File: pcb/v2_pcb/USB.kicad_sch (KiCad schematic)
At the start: 17 parts, among them IC1 AP33772SDKZ-13-FA01, J2 USB_C_Receptacle_USB2.0_16P, Q1 NMOS, Q2 NMOS, U4 TPD8S300ARUKR

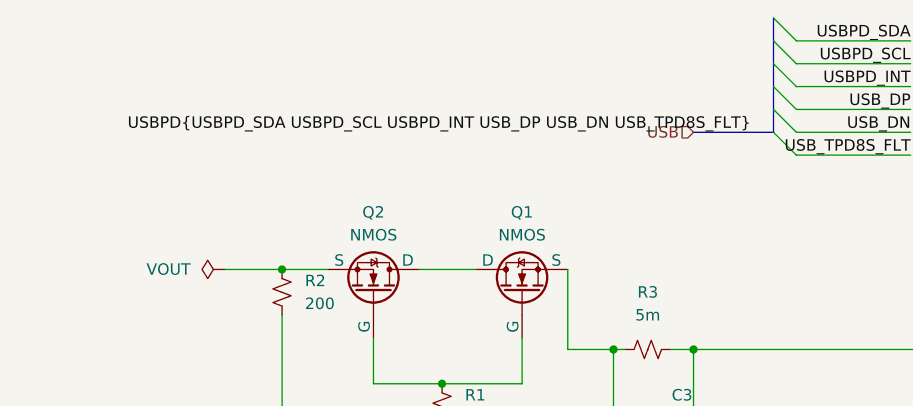
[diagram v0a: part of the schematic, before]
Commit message: done with max17320
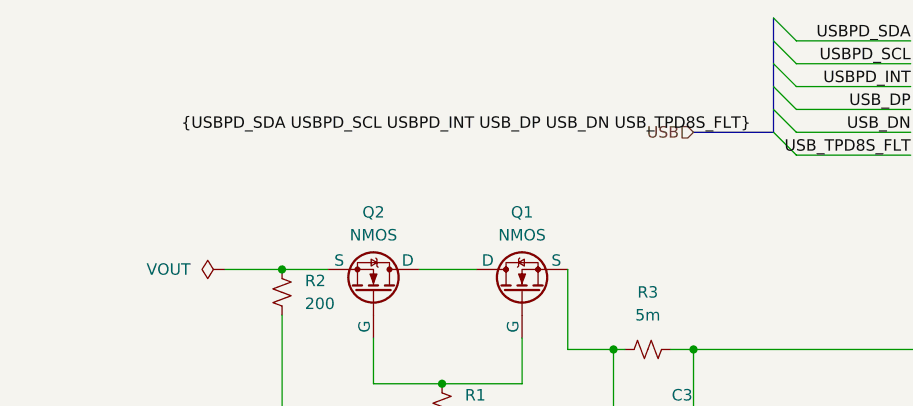
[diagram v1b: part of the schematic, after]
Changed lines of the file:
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@@
 		)
 	)
-	(label "USBPD{USBPD_SDA USBPD_SCL USBPD_INT USB_DP USB_DN USB_TPD8S_FLT}"
+	(label "{USBPD_SDA USBPD_SCL USBPD_INT USB_DP USB_DN USB_TPD8S_FLT}"
 		(at 97.79 50.8 180)
 		(effects

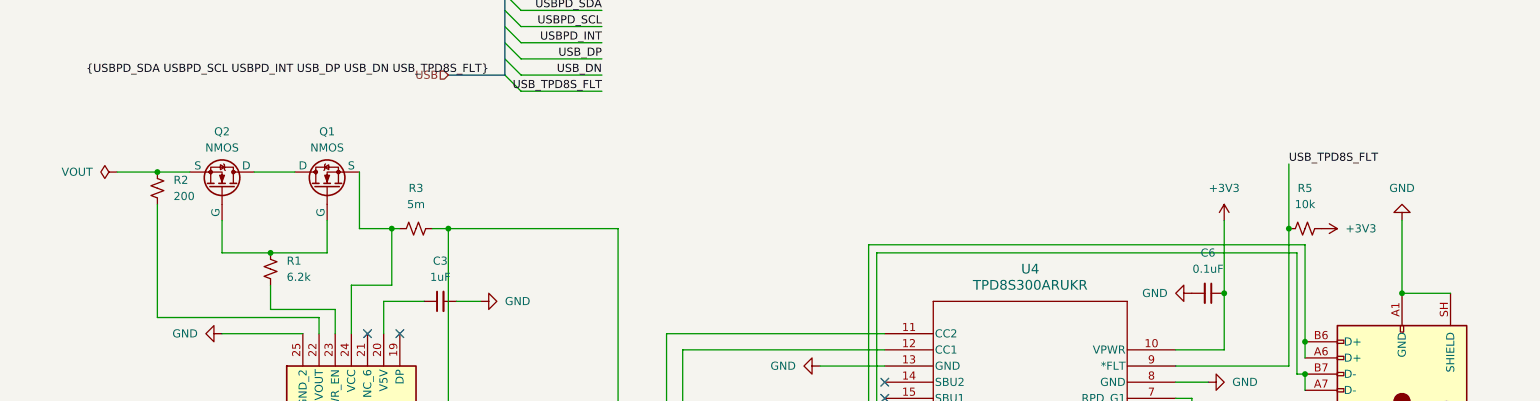
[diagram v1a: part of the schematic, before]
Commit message: add rpls for 1v8, 5v
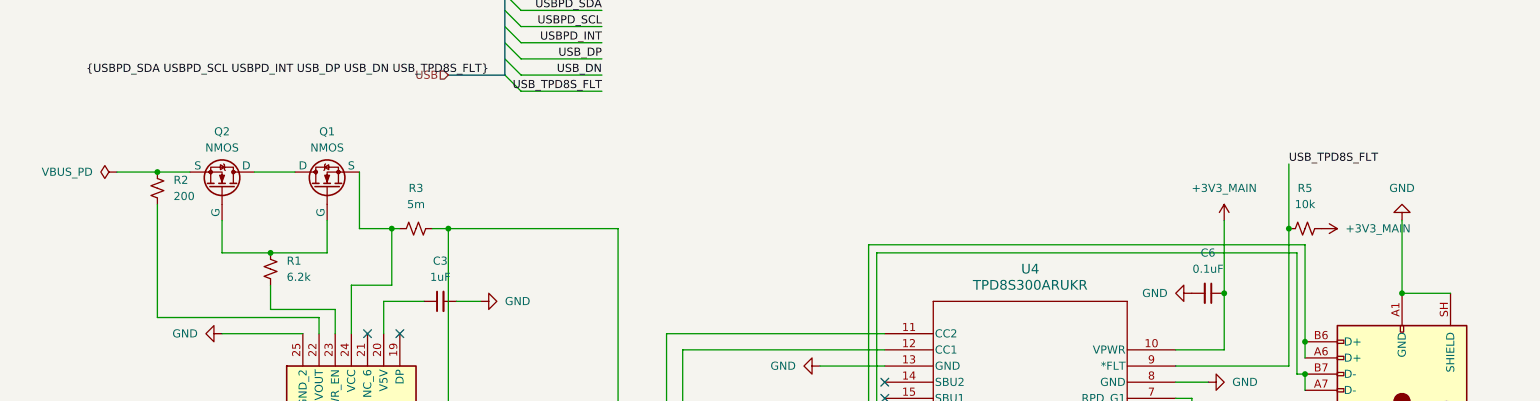
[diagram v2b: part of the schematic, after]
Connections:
- net +3V3 renamed +3V3_MAIN
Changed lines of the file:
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@@
 			)
 		)
-		(property "Value" "+3V3"
+		(property "Value" "+3V3_MAIN"
 			(at 213.36 68.58 0)
 			(show_name no)
@@
 			)
 		)
-		(property "Value" "+3V3"
+		(property "Value" "+3V3_MAIN"
 			(at 232.41 74.9299 90)
 			(show_name no)
@@
 			)
 		)
-		(property "Value" "VOUT"
+		(property "Value" "VBUS_PD"
 			(at 35.56 66.0399 90)
 			(show_name no)

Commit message: pcb done
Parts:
- removed Q1, Q2: NMOS, symbol Simulation_SPICE:NMOS
- added C230: 1uF 35V X7R, Capacitor_SMD:C_0805_2012Metric, symbol Device:C_Small
- added C231, C232: 100nF, Capacitor_SMD:C_0603_1608Metric, symbol Device:C_Small
- added C253: 100nF 10V X7R, Capacitor_SMD:C_0603_1608Metric, symbol Device:C_Small
- added C254: 1nF 10V X7R, Capacitor_SMD:C_0603_1608Metric, symbol Device:C_Small
- added Q1, Q2: CSD18540Q5B, open-race-v2:VSON-CLIP-8_DNK_5x6mm, symbol open-race-v2:CSD18540Q5B
- added R241, R242: 5.1k 1%, Resistor_SMD:R_0603_1608Metric, symbol Device:R_Small_US
- added R243: 10k, Resistor_SMD:R_0603_1608Metric, symbol Device:R_Small_US
- added R249: 100k, Resistor_SMD:R_0603_1608Metric, symbol Device:R_Small_US
- added R250: 88.7k 1%, Resistor_SMD:R_0603_1608Metric, symbol Device:R_Small_US
- added R251: 10.0k 1%, Resistor_SMD:R_0603_1608Metric, symbol Device:R_Small_US
- added U24: TXS0104EPW, Package_SO:TSSOP-14_4.4x5mm_P0.65mm, symbol Logic_LevelTranslator:TXS0104EPW
- added U25: TPS3808G01DBVR, Package_TO_SOT_SMD:SOT-23-6, symbol Power_Supervisor:TPS3808DBV
- C2, C4: footprint (none) -> Capacitor_SMD:C_0603_1608Metric
- C3: value 1uF -> 1uF 10V X7R; footprint (none) -> Capacitor_SMD:C_0805_2012Metric
- C5: value 0.1uF -> 100nF 50V X7R; footprint (none) -> Capacitor_SMD:C_0603_1608Metric
- C6: value 0.1uF -> 1uF 10V X7R; footprint (none) -> Capacitor_SMD:C_0805_2012Metric
- D1: value LED -> LTST-C190KGKT GREEN; footprint (none) -> LED_SMD:LED_0603_1608Metric; MPN (none) -> LTST-C190KGKT
- IC1: footprint AP33772SDKZ13FA01 -> Package_DFN_QFN:WQFN-24-1EP_4x4mm_P0.5mm_EP2.45x2.45mm; MPN (none) -> AP33772SDKZ-13-FA01
- J2: value USB_C_Receptacle_USB2.0_16P -> USB4105-GF-A; footprint (none) -> Connector_USB:USB_C_Receptacle_GCT_USB4105-xx-A_16P_TopMnt_Horizontal; symbol Connector:USB_C_Receptacle_USB2.0_16P -> open-race-v2:USB_C_Receptacle_USB2.0_16P; MPN (none) -> USB4105-GF-A
- R1, R2, R4, R5: footprint (none) -> Resistor_SMD:R_0603_1608Metric
- R3: value 5m -> 5m 1% 1W; footprint (none) -> Resistor_SMD:R_2512_6332Metric; MPN (none) -> WSL2512R0050FEA
- TH1: value 10K@25c -> NCP15XH103F03RC; footprint (none) -> Resistor_SMD:R_0402_1005Metric; MPN (none) -> NCP15XH103F03RC
- U4: footprint WQFN20_RUK_TEX -> Package_DFN_QFN:Texas_RUK0020B_WQFN-20-1EP_3x3mm_P0.4mm_EP1.7x1.7mm; MPN (none) -> TPD8S300ARUKR
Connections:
- net +3V3_MAIN: now also C231.1, C253.1, R243.1, U24.1 (V_{CCA}), U25.3 (~{MR}), U25.6 (VDD)
- net GND: now also C230.2, C231.2, C232.2, C253.2, C254.2, R241.2, R242.2, R249.2, R251.2, U24.7 (GND), U25.2 (GND)
- net USBPD_INT: now also U24.4 (A3); no longer IC1.9 (INT)
- net USBPD_SCL: now also U24.3 (A2); no longer IC1.5 (SCL)
- net USBPD_SDA: now also U24.2 (A1); no longer IC1.4 (SDA)
- net AP_ISENP: now reaches IC1.1 (ISENP), J2.A4 (VBUS), J2.A9 (VBUS), J2.B4 (VBUS), J2.B9 (VBUS), R3.2
- net USB_CC1_PROT: now reaches J2.A5 (CC1), U4.4 (C_CC1), U4.7 (RPD_G1)
- net USB_SBU1_PROT: now reaches J2.A8 (SBU1), U4.1 (C_SBU1)
- net USB_CC2_PROT: now reaches J2.B5 (CC2), U4.5 (C_CC2), U4.6 (RPD_G2)
- net USB_SBU2_PROT: now reaches J2.B8 (SBU2), U4.2 (C_SBU2)
- net AP_LED_DRV: now reaches IC1.8 (LED), R4.1
- net AP_V5V: now reaches C3.1, IC1.20 (V5V)
- net AP_V5V: now also C232.1, R250.1, U24.14 (V_{CCB})
- net AP_OTP: now reaches IC1.13 (OTP), TH1.1
- net AP_IFB: now reaches C2.1, IC1.15 (IFB)
- net CC2_SNK: now reaches IC1.16 (CC2), U4.11 (CC2)
- net CC2_SNK: now also R242.1
- net CC1_SNK: now reaches IC1.17 (CC1), U4.12 (CC1)
- net CC1_SNK: now also R241.1
- net AP_PWR_EN_BIAS: now reaches IC1.22 (VOUT), R2.2
- net AP_VCC_BIAS: now reaches IC1.23 (PWR_EN), R1.2
- net AP_VCC: now reaches IC1.24 (VCC), R3.1
- net AP_VCC: now also C230.1, Q1.1 (S), Q1.2 (S), Q1.3 (S)
- net TPD_VBIAS: now reaches C5.2, U4.3 (VBIAS)
- net VBUS_PD: now reaches R2.1
- net VBUS_PD: now also Q2.1 (S), Q2.2 (S), Q2.3 (S)
- net USB_PD_GATE: now reaches R1.1
- net USB_PD_GATE: now also Q1.4 (G), Q2.4 (G)
- new net AP_USBPD_INT_5V: IC1.9 (INT), U24.11 (B3)
- new net AP_USBPD_SCL_5V: IC1.5 (SCL), U24.12 (B2)
- new net AP_USBPD_SDA_5V: IC1.4 (SDA), U24.13 (B1)
- new net TXS_OE: R243.2, R249.1, U24.8 (OE), U25.1 (~{RESET})
- new net USB_PD_FET_COMMON: Q1.5 (D), Q1.6 (D), Q1.7 (D), Q1.8 (D), Q2.5 (D), Q2.6 (D), Q2.7 (D), Q2.8 (D)
- new net USB_VBUS_SENSE: C254.1, R250.2, R251.1, U25.5 (SENSE)
- no-connect marks 11 -> 16
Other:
- note added: "AP33772 SDA/SCL/INT translated between AP_V5V and +3V3_MAIN; TPD8S300 FLT remains 3V3 open-drain."
- note added: "PRE-LAYOUT HOLD: validate Q1/Q2 dissipation, SOA, copper area and connector/TPD8S300 thermal rise at maximum negotiated current."
- note added: "TXS0104 OE hardware interlock: U25 monitors AP_V5V at ~4.00 V; open-drain RESET plus R243/R249 holds OE low outside the valid VCCA<=VCCB window."
- note added: "USB PD POLICY: SPR/PPS only; firmware request <=20 V (21 V design ceiling). EPR MUST remain disabled."
- note added: "USB_VBUS_SENSE is the U25 divider node (~0.507 V at AP_V5V=5 V); MCU ADC must use a long sample time."

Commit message: switch mosfets
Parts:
- Q1, Q2: value CSD18540Q5B -> NMOS
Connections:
- net USB_PD_GATE is gone; now on net USB_PD_FET_COMMON: Q1.4 (G), Q2.4 (G), R1.1

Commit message: power and debug cleanup
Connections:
- net USB_PD_FET_COMMON: no longer Q1.4 (G), Q2.4 (G), R1.1
- new net USB_PD_GATE: Q1.4 (G), Q2.4 (G), R1.1

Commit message: fix minor
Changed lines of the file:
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@@
-	(wire
-		(pts
-			(xy 76.2 91.44) (xy 106.68 83.82)
-		)
-		(stroke
-			(width 0)
-			(type default)
-		)
-	)
 	(wire
 		(pts
@@
 	(wire
 		(pts
-			(xy 106.68 83.82) (xy 77.47 66.04)
-		)
-		(stroke
+			(xy 82.55 83.82) (xy 106.68 83.82)
+		)
+		(stroke
